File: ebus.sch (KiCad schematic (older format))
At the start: 45 parts, among them J1 EBUS, J2 UART, J3 USB_B_Micro, J4 PWR, J5 SERVICE, J6 PROG, Q1 BC337, U1 LM393, U2 4N25, U3 L7805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

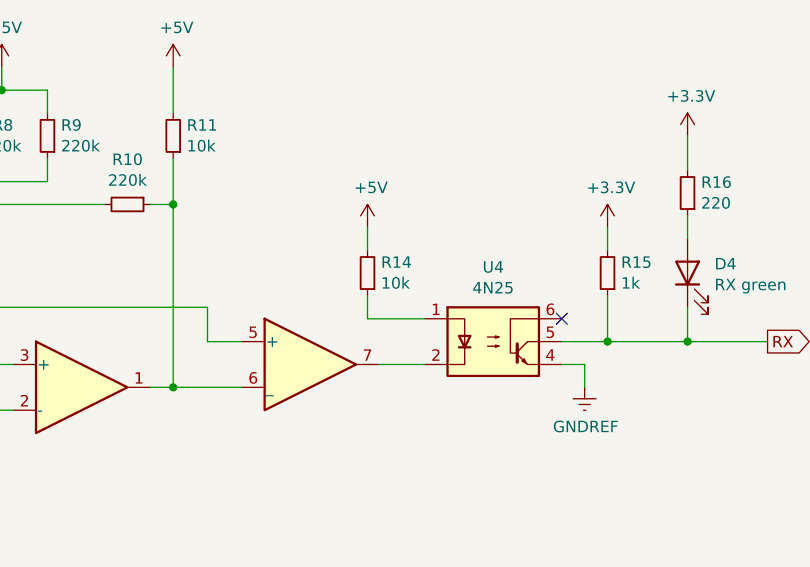
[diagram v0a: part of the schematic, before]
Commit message: Mistake in R14 resistor value fix
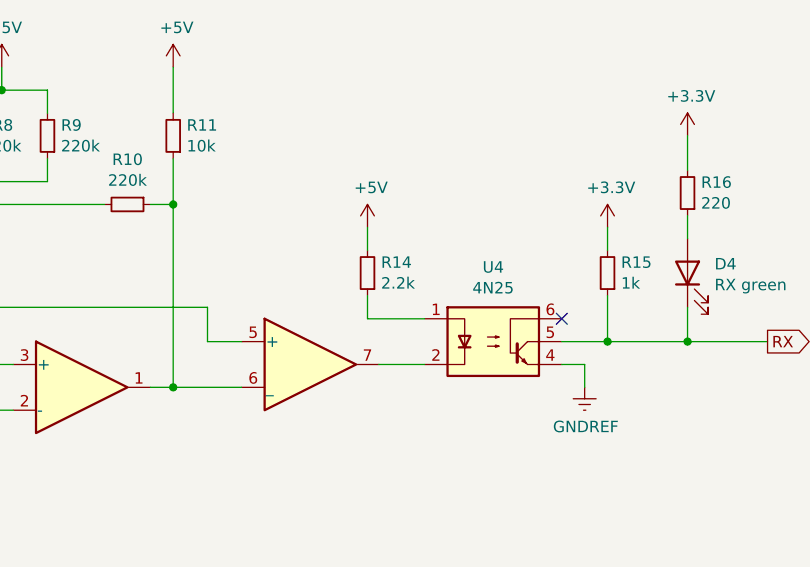
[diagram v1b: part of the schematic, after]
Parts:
- C2, C4: footprint Capacitor_SMD:C_1210_3225Metric -> Capacitor_SMD:C_1206_3216Metric
- R14: value 10k -> 2.2k
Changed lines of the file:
@@
 P 3250 4500
 F 0 "R14" H 3191 4454 50  0000 R CNN
-F 1 "10k" H 3191 4545 50  0000 R CNN
+F 1 "2.2k" H 3191 4545 50  0000 R CNN
 F 2 "Resistor_THT:R_Axial_DIN0207_L6.3mm_D2.5mm_P7.62mm_Horizontal" H 3250 4500 50  0001 C CNN
 F 3 "~" H 3250 4500 50  0001 C CNN
@@
 F 0 "C2" H 8042 2346 50  0000 L CNN
 F 1 "100nF" H 8042 2255 50  0000 L CNN
-F 2 "Capacitor_SMD:C_1210_3225Metric" H 7950 2300 50  0001 C CNN
+F 2 "Capacitor_SMD:C_1206_3216Metric" H 7950 2300 50  0001 C CNN
 F 3 "~" H 7950 2300 50  0001 C CNN
 	1    7950 2300
@@
 F 0 "C4" H 9742 2346 50  0000 L CNN
 F 1 "100nF" H 9742 2255 50  0000 L CNN
-F 2 "Capacitor_SMD:C_1210_3225Metric" H 9650 2300 50  0001 C CNN
+F 2 "Capacitor_SMD:C_1206_3216Metric" H 9650 2300 50  0001 C CNN
 F 3 "~" H 9650 2300 50  0001 C CNN
 	1    9650 2300
